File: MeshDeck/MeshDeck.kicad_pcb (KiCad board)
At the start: 4 copper layers, 48 parts, among them CN1 ATGM336H-6N-74, SW1 4*4*1.7, SW2 4*4*1.7, U1 ESP32-S3-WROOM-1(N16R8), U2 SX1262S8S+T-X1, U3 TPS6282533DMQR, U4 BQ24074RGTR, U5 RN32768114

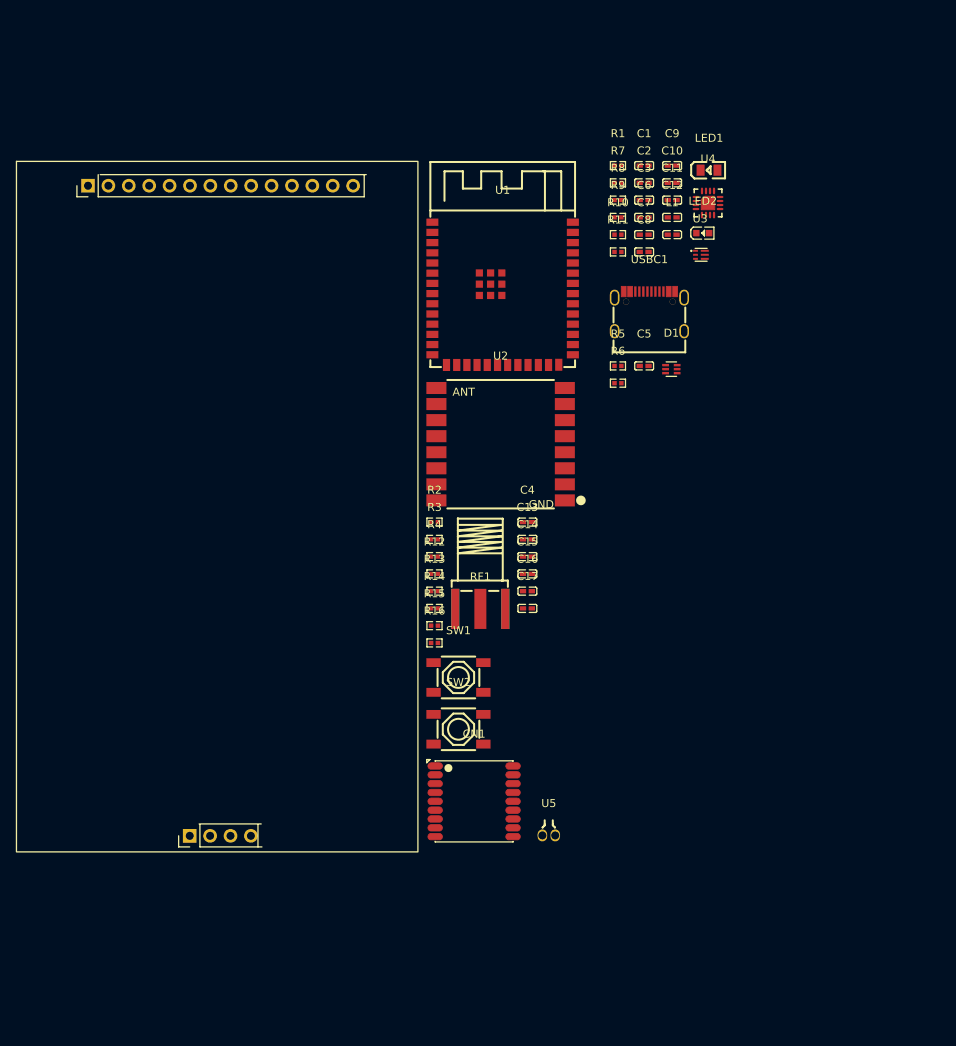
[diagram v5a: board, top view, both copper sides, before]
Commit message: Added GPS and sof power button
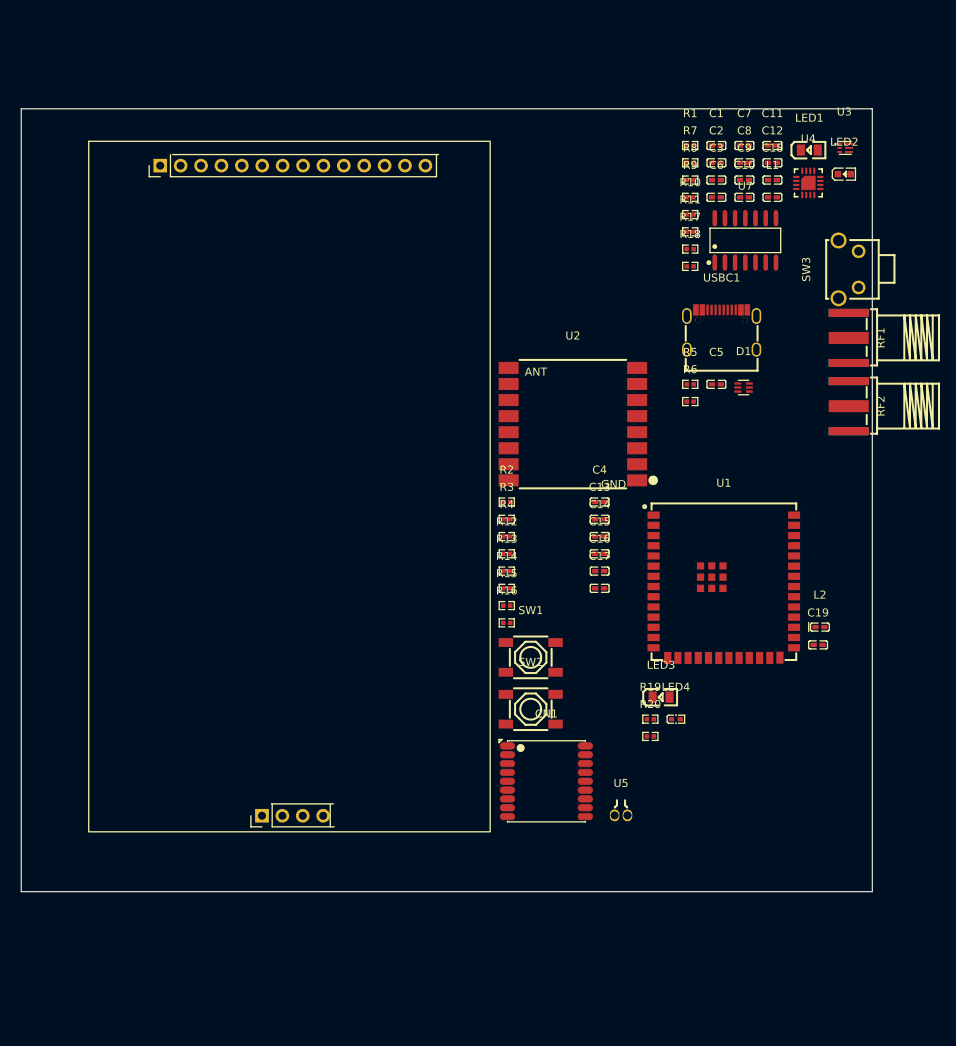
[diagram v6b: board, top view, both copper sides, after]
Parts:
- added C18: 1uF, MeshDeck:C0402, F.Cu at (183.6, 51.4)
- added C19: 10uF, MeshDeck:C0402, F.Cu at (189.2, 109.3)
- added L2: 47nH, MeshDeck:L0402-RD, F.Cu at (189.5, 107.0)
- added LED3: 0805G (Green), MeshDeck:LED0805-R-RD, F.Cu at (169.7, 115.8)
- added LED4: red, MeshDeck:LED0402-RD, F.Cu at (171.5, 118.5)
- added R17: 10KOhm, MeshDeck:R0402, F.Cu at (173.3, 60.0)
- added R18: 10KOhm, MeshDeck:R0402, F.Cu at (173.3, 62.1)
- added R19: 220ohm, MeshDeck:R0402, F.Cu at (168.3, 118.5)
- added R20: 220ohm, MeshDeck:R0402, F.Cu at (168.3, 120.7)
- added RF2: HJ-SMA023, MeshDeck:SMA-SMD_HJ-SMA023, F.Cu at (193.1, 79.5)
- added SW3: SKHHLVA010, MeshDeck:KEY-TH_4P-L7.5-W6.8-P4.50-LS7.2, F.Cu at (193.0, 62.5)
- added U7: CD4013BM, MeshDeck:SOIC-14_L8.7-W3.9-P1.27-LS6.0-BL, F.Cu at (180.2, 58.9)
- U1: value ESP32-S3-WROOM-1(N16R8) -> ESP32-S3-WROOM-1U-N16R8; footprint MeshDeck:WIRELM-SMD_ESP32-S3-WROOM-1 -> MeshDeck:WIRELM-SMD_ESP32-S3-WROOM-1U
- moved RF1 57.0 mm to (193.1, 71.0), turned to -90 degrees
- moved U1 45.7 mm to (177.5, 102.0)
- moved U3 22.4 mm to (192.5, 47.4)
- moved LED2 19.1 mm to (192.5, 50.6)
- moved C8 16.7 mm to (180.1, 49.2)
- moved C7 16.7 mm to (180.1, 47.1)
- moved C11 14.2 mm to (183.6, 47.1)
- moved C12 14.2 mm to (183.6, 49.2)
- moved L1 13.3 mm to (183.6, 53.5)
- moved LED1 12.7 mm to (188.1, 47.6)
- moved U4 12.7 mm to (188.0, 51.7)
- moved C1 9.34 mm to (176.6, 47.1)
- moved C13 9.34 mm to (162.0, 93.6)
- moved C14 9.34 mm to (162.0, 95.8)
- moved C15 9.34 mm to (162.0, 97.9)
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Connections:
- CN1 pad 1: unconnected-(CN1-GND-Pad1) -> GND
- CN1 pad 10: unconnected-(CN1-GND-Pad10) -> GND
- CN1 pad 11: unconnected-(CN1-RF_IN-Pad11) -> Net-(CN1-RF_IN)
- CN1 pad 12: unconnected-(CN1-GND-Pad12) -> GND
- CN1 pad 14: unconnected-(CN1-VCC_RF-Pad14) -> Net-(CN1-VCC_RF)
- CN1 pad 2: unconnected-(CN1-TXD0-Pad2) -> /RXD0_ESP
- CN1 pad 3: unconnected-(CN1-RXD0-Pad3) -> /RXD0_ESP
- CN1 pad 4: unconnected-(CN1-1PPS-Pad4) -> /IO3
- CN1 pad 5: unconnected-(CN1-ON/OFF-Pad5) -> /IO48
- CN1 pad 6: unconnected-(CN1-VBAT-Pad6) -> /3V3
- CN1 pad 8: unconnected-(CN1-VCC-Pad8) -> /3V3
- CN1 pad 9: unconnected-(CN1-nRESET-Pad9) -> /IO35
- U1 pad 15: unconnected-(U1-IO3-Pad15) -> /IO3
- U1 pad 16: unconnected-(U1-IO46-Pad16) -> GND
- U1 pad 18: unconnected-(U1-IO10-Pad18) -> /IO10
- U1 pad 23: unconnected-(U1-IO21-Pad23) -> /IO21
- U1 pad 24: unconnected-(U1-IO47-Pad24) -> /IO47
- U1 pad 25: unconnected-(U1-IO48-Pad25) -> /IO48
- U1 pad 28: unconnected-(U1-IO35-Pad28) -> /IO35
- U1 pad 36: unconnected-(U1-RXD0-Pad36) -> /RXD0_ESP
- U1 pad 37: unconnected-(U1-TXD0-Pad37) -> /RXD0_ESP
- U3 pad 1: /Power Sheet/BCC_OUT -> Net-(LED3-A)
- U6 pad 1: unconnected-(U6-VCC-Pad1) -> /3V3
- U6 pad 10: unconnected-(U6-T_CLK-Pad10) -> /SPI.SCK
- U6 pad 11: unconnected-(U6-T_CS-Pad11) -> /IO21
- U6 pad 12: unconnected-(U6-T_MOSI-Pad12) -> /SPI.MOSI
- U6 pad 13: unconnected-(U6-T_MISO-Pad13) -> /SPI.MISO
- U6 pad 14: unconnected-(U6-T_IRQ-Pad14) -> /IO47
- U6 pad 2: unconnected-(U6-GND-Pad2) -> GND
- U6 pad 4: unconnected-(U6-RESET-Pad4) -> /IO10
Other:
- board outline added: 106 x 97.5 mm

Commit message: added sd card and started keyboard
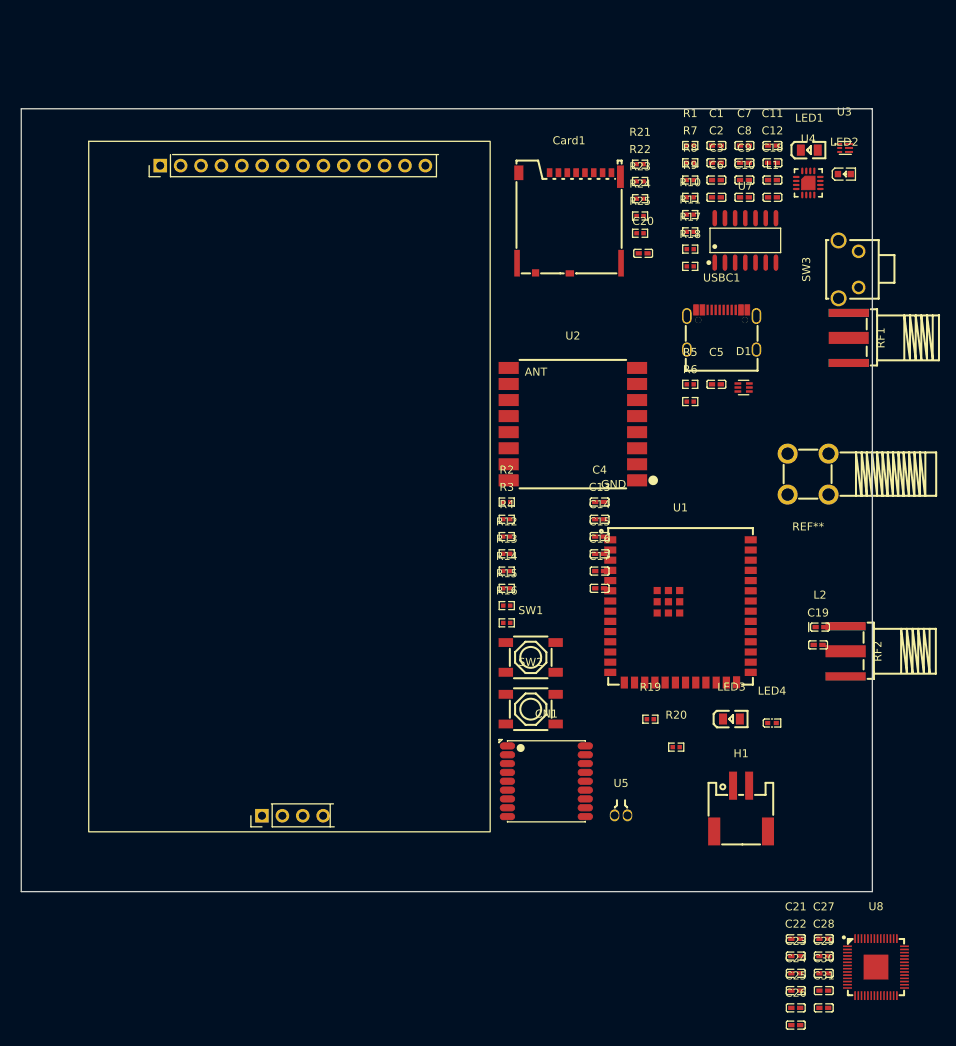
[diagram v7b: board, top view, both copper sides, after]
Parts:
- added C20: 0.1uF, MeshDeck:C0402, F.Cu at (167.4, 60.5)
- added C21: 1uF, MeshDeck:C0402, F.Cu at (186.5, 145.9)
- added C22: 0.1uF, MeshDeck:C0402, F.Cu at (186.5, 148.0)
- added C23: 0.1uF, MeshDeck:C0402, F.Cu at (186.5, 150.2)
- added C24: 0.1uF, MeshDeck:C0402, F.Cu at (186.5, 152.3)
- added C25: 0.1uF, MeshDeck:C0402, F.Cu at (186.5, 154.5)
- added C26: 0.1uF, MeshDeck:C0402, F.Cu at (186.5, 156.6)
- added C27: 0.1uF, MeshDeck:C0402, F.Cu at (189.9, 145.9)
- added C28: 0.1uF, MeshDeck:C0402, F.Cu at (189.9, 148.0)
- added C29: 1uF, MeshDeck:C0402, F.Cu at (189.9, 150.2)
- added C30: 0.1uF, MeshDeck:C0402, F.Cu at (189.9, 152.3)
- added C31: 0.1uF, MeshDeck:C0402, F.Cu at (189.9, 154.5)
- added Card1: 503398-1892, MeshDeck:TF-SMD_503398-1892, F.Cu at (158.2, 56.7)
- added H1: WAFER-PH2.0-2PWB, MeshDeck:CONN-SMD_2P-P2.00_XUNPU_WAFER-PH2.0-2PWB, F.Cu at (179.7, 129.7)
- added R21: 10KOhm, MeshDeck:R0402, F.Cu at (167.1, 49.4)
- added R22: 10KOhm, MeshDeck:R0402, F.Cu at (167.1, 51.5)
- added R23: 10KOhm, MeshDeck:R0402, F.Cu at (167.1, 53.7)
- added R24: 10KOhm, MeshDeck:R0402, F.Cu at (167.1, 55.9)
- added R25: 10KOhm, MeshDeck:R0402, F.Cu at (167.1, 58.0)
- added REF**: SMA-TH_HJ-SMA429, MeshDeck:SMA-TH_HJ-SMA429, F.Cu at (188.0, 88.0)
- added U8: RP2040, MeshDeck:LQFN-56_L7.0-W7.0-P0.4-EP, F.Cu at (196.4, 149.4)
- moved RF2 30.5 mm to (192.7, 110.1)
- moved LED4 12.0 mm to (183.5, 119.0)
- moved LED3 9.18 mm to (178.4, 118.5)
- moved U1 6.21 mm to (172.1, 105.1)
- moved R20 3.48 mm to (171.6, 122.0)
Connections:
- SW3 pad 2: Net-(LED4-A) -> /Power Sheet/CLOCK1
- U1 pad 29: unconnected-(U1-IO36-Pad29) -> /IO36
- U7 pad 3: Net-(LED4-A) -> /Power Sheet/CLOCK1

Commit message: started pcb plus pin socket for expansion
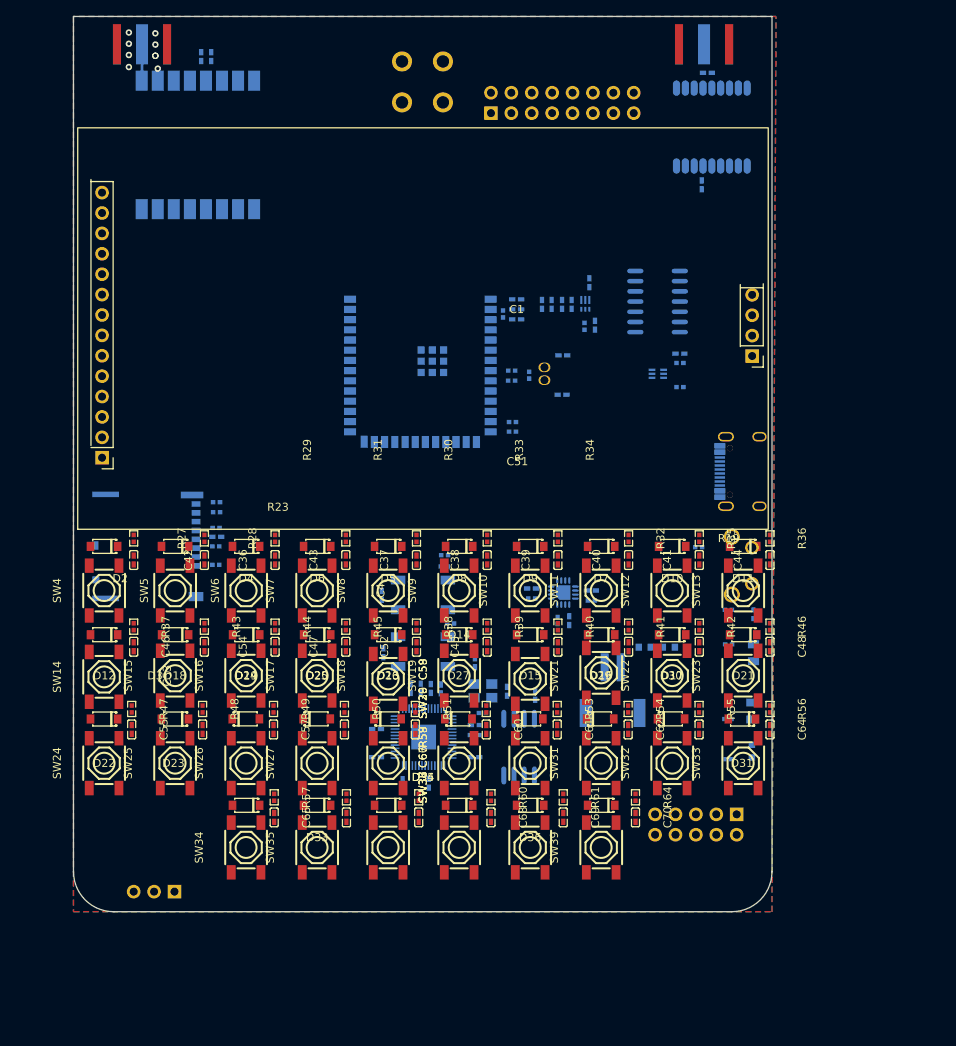
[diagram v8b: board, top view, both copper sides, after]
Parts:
- added C32: 0.1uF, MeshDeck:C0402, B.Cu at (154.0, 115.5)
- added C33: 15pF, MeshDeck:C0402, B.Cu at (146.5, 111.5)
- added C34: 15pF, MeshDeck:C0402, B.Cu at (150.5, 115.0)
- added C35: 0.1uF, MeshDeck:C0402, F.Cu at (104.0, 98.7)
- added C36: 0.1uF, MeshDeck:C0402, F.Cu at (121.6, 98.7)
- added C37: 0.1uF, MeshDeck:C0402, F.Cu at (139.2, 98.7)
- added C38: 0.1uF, MeshDeck:C0402, F.Cu at (148.0, 98.7)
- added C39: 0.1uF, MeshDeck:C0402, F.Cu at (156.8, 98.7)
- added C40: 0.1uF, MeshDeck:C0402, F.Cu at (165.6, 98.7)
- added C41: 0.1uF, MeshDeck:C0402, F.Cu at (174.4, 98.7)
- added C42: 0.1uF, MeshDeck:C0402, F.Cu at (112.8, 98.7)
- added C43: 0.1uF, MeshDeck:C0402, F.Cu at (130.4, 98.7)
- added C44: 0.1uF, MeshDeck:C0402, F.Cu at (183.2, 98.7)
- added C45: 0.1uF, MeshDeck:C0402, F.Cu at (148.0, 109.5)
- added C46: 0.1uF, MeshDeck:C0402, F.Cu at (104.0, 109.5)
- added C47: 0.1uF, MeshDeck:C0402, F.Cu at (130.4, 109.5)
- added C48: 0.1uF, MeshDeck:C0402, F.Cu at (183.2, 109.5)
- added C49: 0.1uF, MeshDeck:C0402, F.Cu at (174.4, 109.5)
- added C50: 0.1uF, MeshDeck:C0402, F.Cu at (165.6, 109.5)
- added C51: 0.1uF, MeshDeck:C0402, F.Cu at (156.8, 109.5)
- added C52: 0.1uF, MeshDeck:C0402, F.Cu at (139.2, 109.5)
- added C53: 0.1uF, MeshDeck:C0402, F.Cu at (112.8, 109.5)
- added C54: 0.1uF, MeshDeck:C0402, F.Cu at (121.6, 109.5)
- added C55: 0.1uF, MeshDeck:C0402, F.Cu at (103.8, 119.8)
- added C56: 0.1uF, MeshDeck:C0402, F.Cu at (112.6, 119.8)
- added C57: 0.1uF, MeshDeck:C0402, F.Cu at (121.4, 119.8)
- added C58: 0.1uF, MeshDeck:C0402, F.Cu at (130.2, 119.8)
- added C59: 0.1uF, MeshDeck:C0402, F.Cu at (139.1, 119.8)
- added C60: 0.1uF, MeshDeck:C0402, F.Cu at (147.9, 119.8)
- added C61: 0.1uF, MeshDeck:C0402, F.Cu at (156.8, 119.8)
- added C62: 0.1uF, MeshDeck:C0402, F.Cu at (165.6, 119.8)
- added C63: 0.1uF, MeshDeck:C0402, F.Cu at (174.4, 119.8)
- added C64: 0.1uF, MeshDeck:C0402, F.Cu at (183.2, 119.8)
- added C65: 0.1uF, MeshDeck:C0402, F.Cu at (121.5, 130.8)
- added C66: 0.1uF, MeshDeck:C0402, F.Cu at (130.5, 130.8)
- added C67: 0.1uF, MeshDeck:C0402, F.Cu at (139.5, 130.8)
- added C68: 0.1uF, MeshDeck:C0402, F.Cu at (148.5, 130.8)
- added C69: 0.1uF, MeshDeck:C0402, F.Cu at (157.5, 130.8)
- added C70: 0.1uF, MeshDeck:C0402, F.Cu at (166.5, 130.8)
- added D10: 1N4148W T4, MeshDeck:SOD-123_L2.8-W1.8-LS3.7-RD, F.Cu at (171.1, 97.0)
- added D11: 1N4148W T4, MeshDeck:SOD-123_L2.8-W1.8-LS3.7-RD, F.Cu at (179.9, 97.0)
- added D12: 1N4148W T4, MeshDeck:SOD-123_L2.8-W1.8-LS3.7-RD, F.Cu at (100.3, 108.0)
- added D13: 1N4148W T4, MeshDeck:SOD-123_L2.8-W1.8-LS3.7-RD, F.Cu at (135.7, 108.0)
- added D14: 1N4148W T4, MeshDeck:SOD-123_L2.8-W1.8-LS3.7-RD, F.Cu at (144.5, 108.0)
- added D15: 1N4148W T4, MeshDeck:SOD-123_L2.8-W1.8-LS3.7-RD, F.Cu at (153.4, 108.0)
- added D16: 1N4148W T4, MeshDeck:SOD-123_L2.8-W1.8-LS3.7-RD, F.Cu at (162.2, 108.0)
- added D17: 1N4148W T4, MeshDeck:SOD-123_L2.8-W1.8-LS3.7-RD, F.Cu at (171.1, 108.0)
- added D18: 1N4148W T4, MeshDeck:SOD-123_L2.8-W1.8-LS3.7-RD, F.Cu at (109.2, 108.0)
- added D19: 1N4148W T4, MeshDeck:SOD-123_L2.8-W1.8-LS3.7-RD, F.Cu at (118.0, 108.0)
- added D2: 1N4148W T4, MeshDeck:SOD-123_L2.8-W1.8-LS3.7-RD, F.Cu at (100.3, 97.0)
- added D20: 1N4148W T4, MeshDeck:SOD-123_L2.8-W1.8-LS3.7-RD, F.Cu at (126.8, 108.0)
- added D21: 1N4148W T4, MeshDeck:SOD-123_L2.8-W1.8-LS3.7-RD, F.Cu at (179.9, 108.0)
- added D22: 1N4148W T4, MeshDeck:SOD-123_L2.8-W1.8-LS3.7-RD, F.Cu at (100.3, 118.5)
- added D23: 1N4148W T4, MeshDeck:SOD-123_L2.8-W1.8-LS3.7-RD, F.Cu at (109.1, 118.5)
- added D24: 1N4148W T4, MeshDeck:SOD-123_L2.8-W1.8-LS3.7-RD, F.Cu at (118.0, 118.5)
- added D25: 1N4148W T4, MeshDeck:SOD-123_L2.8-W1.8-LS3.7-RD, F.Cu at (126.8, 118.5)
- added D26: 1N4148W T4, MeshDeck:SOD-123_L2.8-W1.8-LS3.7-RD, F.Cu at (135.6, 118.5)
- added D27: 1N4148W T4, MeshDeck:SOD-123_L2.8-W1.8-LS3.7-RD, F.Cu at (144.4, 118.5)
- added D28: 1N4148W T4, MeshDeck:SOD-123_L2.8-W1.8-LS3.7-RD, F.Cu at (153.3, 118.5)
- added D29: 1N4148W T4, MeshDeck:SOD-123_L2.8-W1.8-LS3.7-RD, F.Cu at (162.1, 118.5)
- added D3: 1N4148W T4, MeshDeck:SOD-123_L2.8-W1.8-LS3.7-RD, F.Cu at (109.2, 97.0)
- added D30: 1N4148W T4, MeshDeck:SOD-123_L2.8-W1.8-LS3.7-RD, F.Cu at (170.9, 118.5)
- added D31: 1N4148W T4, MeshDeck:SOD-123_L2.8-W1.8-LS3.7-RD, F.Cu at (179.8, 118.5)
- added D32: 1N4148W T4, MeshDeck:SOD-123_L2.8-W1.8-LS3.7-RD, F.Cu at (118.0, 129.2)
- added D33: 1N4148W T4, MeshDeck:SOD-123_L2.8-W1.8-LS3.7-RD, F.Cu at (126.8, 129.2)
- added D34: 1N4148W T4, MeshDeck:SOD-123_L2.8-W1.8-LS3.7-RD, F.Cu at (135.7, 129.2)
- added D35: 1N4148W T4, MeshDeck:SOD-123_L2.8-W1.8-LS3.7-RD, F.Cu at (144.5, 129.2)
- added D36: 1N4148W T4, MeshDeck:SOD-123_L2.8-W1.8-LS3.7-RD, F.Cu at (153.4, 129.2)
- added D37: 1N4148W T4, MeshDeck:SOD-123_L2.8-W1.8-LS3.7-RD, F.Cu at (162.2, 129.2)
- added D4: 1N4148W T4, MeshDeck:SOD-123_L2.8-W1.8-LS3.7-RD, F.Cu at (118.0, 97.0)
- added D5: 1N4148W T4, MeshDeck:SOD-123_L2.8-W1.8-LS3.7-RD, F.Cu at (135.7, 97.0)
- added D6: 1N4148W T4, MeshDeck:SOD-123_L2.8-W1.8-LS3.7-RD, F.Cu at (126.8, 97.0)
- added D7: 1N4148W T4, MeshDeck:SOD-123_L2.8-W1.8-LS3.7-RD, F.Cu at (162.2, 97.0)
- added D8: 1N4148W T4, MeshDeck:SOD-123_L2.8-W1.8-LS3.7-RD, F.Cu at (144.5, 97.0)
- added D9: 1N4148W T4, MeshDeck:SOD-123_L2.8-W1.8-LS3.7-RD, F.Cu at (153.4, 97.0)
- added J1: Conn_01x03_MountingPin, Connector_PinHeader_2.54mm:PinHeader_1x03_P2.54mm_Horizontal, B.Cu at (109.1, 140.0)
- added J2: Conn_02x05_Odd_Even, Connector_PinSocket_2.54mm:PinSocket_2x05_P2.54mm_Horizontal, B.Cu at (179.1, 130.4)
- added J3: Conn_02x08_Odd_Even, Connector_PinSocket_2.54mm:PinSocket_2x08_P2.54mm_Horizontal, B.Cu at (148.5, 43.0)
- added R26: 1k, MeshDeck:R0402, B.Cu at (147.4, 117.8)
- added R27: 1k, MeshDeck:R0402, F.Cu at (104.0, 96.0)
- added R28: 1k, MeshDeck:R0402, F.Cu at (112.8, 96.0)
- added R29: 1k, MeshDeck:R0402, F.Cu at (121.6, 96.0)
- added R30: 1k, MeshDeck:R0402, F.Cu at (139.2, 96.0)
- added R31: 1k, MeshDeck:R0402, F.Cu at (130.4, 96.0)
- added R32: 1k, MeshDeck:R0402, F.Cu at (165.6, 96.0)
- added R33: 1k, MeshDeck:R0402, F.Cu at (148.0, 96.0)
- added R34: 1k, MeshDeck:R0402, F.Cu at (156.8, 96.0)
- added R35: 1k, MeshDeck:R0402, F.Cu at (174.4, 96.0)
- added R36: 1k, MeshDeck:R0402, F.Cu at (183.2, 96.0)
- added R37: 1k, MeshDeck:R0402, F.Cu at (104.0, 107.0)
- added R38: 1k, MeshDeck:R0402, F.Cu at (139.2, 107.0)
- added R39: 1k, MeshDeck:R0402, F.Cu at (148.0, 107.0)
- added R40: 1k, MeshDeck:R0402, F.Cu at (156.8, 107.0)
- added R41: 1k, MeshDeck:R0402, F.Cu at (165.6, 107.0)
- added R42: 1k, MeshDeck:R0402, F.Cu at (174.4, 107.0)
- added R43: 1k, MeshDeck:R0402, F.Cu at (112.8, 107.0)
- added R44: 1k, MeshDeck:R0402, F.Cu at (121.6, 107.0)
- added R45: 1k, MeshDeck:R0402, F.Cu at (130.4, 107.0)
- added R46: 1k, MeshDeck:R0402, F.Cu at (183.2, 107.0)
- added R47: 1k, MeshDeck:R0402, F.Cu at (103.8, 117.2)
- added R48: 1k, MeshDeck:R0402, F.Cu at (112.6, 117.2)
- added R49: 1k, MeshDeck:R0402, F.Cu at (121.4, 117.2)
- added R50: 1k, MeshDeck:R0402, F.Cu at (130.2, 117.2)
- added R51: 1k, MeshDeck:R0402, F.Cu at (139.1, 117.2)
- added R52: 1k, MeshDeck:R0402, F.Cu at (147.9, 117.2)
- added R53: 1k, MeshDeck:R0402, F.Cu at (156.8, 117.2)
- added R54: 1k, MeshDeck:R0402, F.Cu at (165.6, 117.2)
- added R55: 1k, MeshDeck:R0402, F.Cu at (174.4, 117.2)
- added R56: 1k, MeshDeck:R0402, F.Cu at (183.2, 117.2)
- added R57: 1k, MeshDeck:R0402, F.Cu at (121.5, 128.2)
- added R58: 1k, MeshDeck:R0402, F.Cu at (130.5, 128.2)
- added R59: 1k, MeshDeck:R0402, F.Cu at (139.5, 128.2)
- added R60: 1k, MeshDeck:R0402, F.Cu at (148.5, 128.2)
- added R61: 1k, MeshDeck:R0402, F.Cu at (157.5, 128.2)
- added R62: 100k, MeshDeck:R0603, B.Cu at (167.7, 109.5)
- added R63: 100k, MeshDeck:R0603, B.Cu at (170.7, 109.5)
- added R64: 1k, MeshDeck:R0402, F.Cu at (166.5, 128.2)
- added SW10: 4*4*1.7, MeshDeck:SW-SMD_4P-L5.2-W5.2-P3.70-LS6.5, F.Cu at (153.4, 102.5)
- added SW11: 4*4*1.7, MeshDeck:SW-SMD_4P-L5.2-W5.2-P3.70-LS6.5, F.Cu at (162.2, 102.5)
- added SW12: 4*4*1.7, MeshDeck:SW-SMD_4P-L5.2-W5.2-P3.70-LS6.5, F.Cu at (171.1, 102.5)
- added SW13: 4*4*1.7, MeshDeck:SW-SMD_4P-L5.2-W5.2-P3.70-LS6.5, F.Cu at (179.9, 102.5)
- added SW14: 4*4*1.7, MeshDeck:SW-SMD_4P-L5.2-W5.2-P3.70-LS6.5, F.Cu at (100.3, 113.2)
- added SW15: 4*4*1.7, MeshDeck:SW-SMD_4P-L5.2-W5.2-P3.70-LS6.5, F.Cu at (109.2, 113.1)
- added SW16: 4*4*1.7, MeshDeck:SW-SMD_4P-L5.2-W5.2-P3.70-LS6.5, F.Cu at (118.0, 113.1)
- added SW17: 4*4*1.7, MeshDeck:SW-SMD_4P-L5.2-W5.2-P3.70-LS6.5, F.Cu at (126.8, 113.1)
- added SW18: 4*4*1.7, MeshDeck:SW-SMD_4P-L5.2-W5.2-P3.70-LS6.5, F.Cu at (135.7, 113.5)
- added SW19: 4*4*1.7, MeshDeck:SW-SMD_4P-L5.2-W5.2-P3.70-LS6.5, F.Cu at (144.5, 113.1)
- added SW20: 4*4*1.7, MeshDeck:SW-SMD_4P-L5.2-W5.2-P3.70-LS6.5, F.Cu at (153.4, 113.5)
- added SW21: 4*4*1.7, MeshDeck:SW-SMD_4P-L5.2-W5.2-P3.70-LS6.5, F.Cu at (162.2, 112.8)
- added SW22: 4*4*1.7, MeshDeck:SW-SMD_4P-L5.2-W5.2-P3.70-LS6.5, F.Cu at (171.1, 113.1)
- added SW23: 4*4*1.7, MeshDeck:SW-SMD_4P-L5.2-W5.2-P3.70-LS6.5, F.Cu at (179.9, 113.1)
- added SW24: 4*4*1.7, MeshDeck:SW-SMD_4P-L5.2-W5.2-P3.70-LS6.5, F.Cu at (100.3, 124.0)
- added SW25: 4*4*1.7, MeshDeck:SW-SMD_4P-L5.2-W5.2-P3.70-LS6.5, F.Cu at (109.2, 124.0)
- added SW26: 4*4*1.7, MeshDeck:SW-SMD_4P-L5.2-W5.2-P3.70-LS6.5, F.Cu at (118.0, 124.0)
- added SW27: 4*4*1.7, MeshDeck:SW-SMD_4P-L5.2-W5.2-P3.70-LS6.5, F.Cu at (126.8, 124.0)
- added SW28: 4*4*1.7, MeshDeck:SW-SMD_4P-L5.2-W5.2-P3.70-LS6.5, F.Cu at (135.7, 124.0)
- added SW29: 4*4*1.7, MeshDeck:SW-SMD_4P-L5.2-W5.2-P3.70-LS6.5, F.Cu at (144.5, 124.0)
- added SW30: 4*4*1.7, MeshDeck:SW-SMD_4P-L5.2-W5.2-P3.70-LS6.5, F.Cu at (153.4, 124.0)
- added SW31: 4*4*1.7, MeshDeck:SW-SMD_4P-L5.2-W5.2-P3.70-LS6.5, F.Cu at (162.2, 124.0)
- added SW32: 4*4*1.7, MeshDeck:SW-SMD_4P-L5.2-W5.2-P3.70-LS6.5, F.Cu at (171.1, 124.0)
- added SW33: 4*4*1.7, MeshDeck:SW-SMD_4P-L5.2-W5.2-P3.70-LS6.5, F.Cu at (179.9, 124.0)
- added SW34: 4*4*1.7, MeshDeck:SW-SMD_4P-L5.2-W5.2-P3.70-LS6.5, F.Cu at (118.0, 134.5)
- added SW35: 4*4*1.7, MeshDeck:SW-SMD_4P-L5.2-W5.2-P3.70-LS6.5, F.Cu at (126.8, 134.5)
- added SW36: 4*4*1.7, MeshDeck:SW-SMD_4P-L5.2-W5.2-P3.70-LS6.5, F.Cu at (135.7, 134.5)
- added SW37: 4*4*1.7, MeshDeck:SW-SMD_4P-L5.2-W5.2-P3.70-LS6.5, F.Cu at (144.5, 134.5)
- added SW38: 4*4*1.7, MeshDeck:SW-SMD_4P-L5.2-W5.2-P3.70-LS6.5, F.Cu at (153.4, 134.5)
- added SW39: 4*4*1.7, MeshDeck:SW-SMD_4P-L5.2-W5.2-P3.70-LS6.5, F.Cu at (162.2, 134.5)
- added SW4: 4*4*1.7, MeshDeck:SW-SMD_4P-L5.2-W5.2-P3.70-LS6.5, F.Cu at (100.3, 102.5)
- added SW5: 4*4*1.7, MeshDeck:SW-SMD_4P-L5.2-W5.2-P3.70-LS6.5, F.Cu at (109.2, 102.5)
- added SW6: 4*4*1.7, MeshDeck:SW-SMD_4P-L5.2-W5.2-P3.70-LS6.5, F.Cu at (118.0, 102.5)
- added SW7: 4*4*1.7, MeshDeck:SW-SMD_4P-L5.2-W5.2-P3.70-LS6.5, F.Cu at (126.8, 102.5)
- added SW8: 4*4*1.7, MeshDeck:SW-SMD_4P-L5.2-W5.2-P3.70-LS6.5, F.Cu at (135.7, 102.5)
- added SW9: 4*4*1.7, MeshDeck:SW-SMD_4P-L5.2-W5.2-P3.70-LS6.5, F.Cu at (144.5, 102.5)
- added U10: ABM8-272-T3_C20625731, MeshDeck:CRYSTAL-SMD_4P-L3.2-W2.5-BL, B.Cu at (147.5, 115.0)
- added U9: W25Q128JVSIQTR, MeshDeck:SOIC-8_L5.3-W5.3-P1.27-LS8.0-BL, B.Cu at (152.0, 122.0)
- C1, C10, C11, C12, C13, C14, C15, C16, C17, C18, C19, C2, C20, C21, C22, C23, C24, C25, C26, C27, C28, C29, C3, C30, C31, C4, C5, C6, C7, C8, C9, CN1, Card1, D1, H1, L1, L2, LED1, LED2, LED3, LED4, R1, R10, R11, R12, R13, R14, R15, R16, R17, R18, R19, R2, R20, R21, R22, R23, R24, R25, R3, R4, R5, R6, R7, R8, R9, REF**, RF1, RF2, SW1, SW2, SW3, U1, U2, U3, U4, U5, U7, U8, USBC1: moved to B.Cu
- moved RF1 95.3 mm to (105.0, 34.5), turned to 180 degrees
- moved CN1 84.1 mm to (176.0, 44.8), turned to 90 degrees
- moved C17 82.0 mm to (113.7, 36.0), turned to -90 degrees
- moved C16 81.1 mm to (112.4, 36.0), turned to -90 degrees
- moved RF2 77.6 mm to (175.0, 34.5), turned to 180 degrees
- moved R7 74.4 mm to (178.0, 123.5), turned to 180 degrees
- moved LED2 72.8 mm to (181.0, 122.5), turned to -90 degrees
- moved L2 70.4 mm to (175.4, 38.0), turned to 180 degrees
- moved LED1 70.2 mm to (181.0, 117.5), turned to -90 degrees
- moved REF** 68.5 mm to (140.0, 39.2), turned to -90 degrees
- moved R23 68.3 mm to (114.2, 97.0), turned to 180 degrees
- moved R21 68.3 mm to (114.3, 92.8), turned to 180 degrees
- moved R22 68.2 mm to (114.3, 94.7), turned to 180 degrees
- moved R8 67.3 mm to (178.0, 118.5)
- moved R25 67.1 mm to (114.2, 99.3), turned to 180 degrees
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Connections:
- net /IO0 renamed /BOOT
- net /IO12 renamed /SCR_CS
- net /IO13 renamed /LORA_BUSY
- net /IO14 renamed /LORA_TXEN
- net /IO17 renamed /LORA_RESET
- net /IO21 renamed /TCH_CS
- net /IO3 renamed /GPS_PPS
- net /IO35 renamed /BOOT_RESET
- net /IO36 renamed /SD_CS
- net /IO45 renamed /LORA_DIO1
- net /IO47 renamed /TCH_IRQ
- CN1 pad 2: /RXD0_ESP -> /LORA_CS
- CN1 pad 3: /RXD0_ESP -> /LORA_CS
- U1 pad 11: unconnected-(U1-IO18-Pad11) -> /IO18
- U1 pad 12: unconnected-(U1-IO8-Pad12) -> /KB_SDA
- U1 pad 17: /IO9 -> /KB_SCL
- U1 pad 30: unconnected-(U1-IO37-Pad30) -> /LORA_CS
- U1 pad 31: unconnected-(U1-IO38-Pad31) -> /IO38
- U1 pad 36: /RXD0_ESP -> /LORA_CS
- U1 pad 37: /RXD0_ESP -> /LORA_CS
- U1 pad 38: unconnected-(U1-IO2-Pad38) -> /IO2
- U1 pad 39: unconnected-(U1-IO1-Pad39) -> /IO1
- U1 pad 4: unconnected-(U1-IO4-Pad4) -> /BTR_LVL
- U1 pad 5: unconnected-(U1-IO5-Pad5) -> /IO5
- U1 pad 6: unconnected-(U1-IO6-Pad6) -> /IO6
- U1 pad 7: unconnected-(U1-IO7-Pad7) -> /IO7
- U2 pad 5: /IO9 -> /LORA_CS
- U8 pad 11: unconnected-(U8-GPIO8-Pad11) -> /Keyboard/COL3
- U8 pad 12: unconnected-(U8-GPIO9-Pad12) -> /Keyboard/COL4
- U8 pad 13: unconnected-(U8-GPIO10-Pad13) -> /Keyboard/COL5
- U8 pad 14: unconnected-(U8-GPIO11-Pad14) -> /Keyboard/COL6
- U8 pad 15: unconnected-(U8-GPIO12-Pad15) -> /Keyboard/COL7
- U8 pad 16: unconnected-(U8-GPIO13-Pad16) -> /Keyboard/COL8
- U8 pad 17: unconnected-(U8-GPIO14-Pad17) -> /Keyboard/COL9
- U8 pad 18: unconnected-(U8-GPIO15-Pad18) -> /Keyboard/COL10
- U8 pad 2: unconnected-(U8-GPIO0-Pad2) -> /Keyboard/GPBOOT
- U8 pad 20: unconnected-(U8-XIN-Pad20) -> /Keyboard/XIN
- U8 pad 21: unconnected-(U8-XOUT-Pad21) -> /Keyboard/XOUT
- U8 pad 24: unconnected-(U8-SWCLK-Pad24) -> Net-(J1-Pin_3)
- U8 pad 25: unconnected-(U8-SWD-Pad25) -> Net-(J1-Pin_1)
- U8 pad 27: unconnected-(U8-GPIO16-Pad27) -> /Keyboard/ROW1
- U8 pad 28: unconnected-(U8-GPIO17-Pad28) -> /Keyboard/ROW2
- U8 pad 29: unconnected-(U8-GPIO18-Pad29) -> /Keyboard/ROW3
- U8 pad 3: unconnected-(U8-GPIO1-Pad3) -> /Keyboard/GPIO1
- U8 pad 30: unconnected-(U8-GPIO19-Pad30) -> /Keyboard/ROW4
- U8 pad 31: unconnected-(U8-GPIO20-Pad31) -> /Keyboard/GPIO20
- U8 pad 32: unconnected-(U8-GPIO21-Pad32) -> /Keyboard/GPTCH_CS
- U8 pad 34: unconnected-(U8-GPIO22-Pad34) -> /Keyboard/GPIO22
- U8 pad 35: unconnected-(U8-GPIO23-Pad35) -> /Keyboard/GPIO23
- U8 pad 36: unconnected-(U8-GPIO24-Pad36) -> /Keyboard/GPIO24
- U8 pad 37: unconnected-(U8-GPIO25-Pad37) -> /Keyboard/GPIO25
- U8 pad 38: unconnected-(U8-GPIO26_ADC0-Pad38) -> /Keyboard/GPIO26_ADC0
- U8 pad 39: unconnected-(U8-GPIO27_ADC1-Pad39) -> /Keyboard/GPIO27_ADC1
- U8 pad 4: unconnected-(U8-GPIO2-Pad4) -> /Keyboard/GPIO2
- U8 pad 40: unconnected-(U8-GPIO28_ADC2-Pad40) -> /Keyboard/GPIO28_ADC2
- U8 pad 41: unconnected-(U8-GPIO29_ADC3-Pad41) -> /Keyboard/GPIO29_ADC3
- U8 pad 5: unconnected-(U8-GPIO3-Pad5) -> /Keyboard/GPGPS_PPS
- U8 pad 51: unconnected-(U8-QSPI_SD3-Pad51) -> /Keyboard/QSPI_SD3
- U8 pad 52: unconnected-(U8-QSPI_SCLK-Pad52) -> /Keyboard/QSPI_SCLK
- U8 pad 53: unconnected-(U8-QSPI_SD0-Pad53) -> /Keyboard/QSPI_SD0
- U8 pad 54: unconnected-(U8-QSPI_SD2-Pad54) -> /Keyboard/QSPI_SD2
- U8 pad 55: unconnected-(U8-QSPI_SD1-Pad55) -> /Keyboard/QSPI_SD1
- U8 pad 56: unconnected-(U8-QSPI_SS-Pad56) -> /3V3
- U8 pad 6: unconnected-(U8-GPIO4-Pad6) -> /KB_SDA
- U8 pad 7: unconnected-(U8-GPIO5-Pad7) -> /KB_SCL
- U8 pad 8: unconnected-(U8-GPIO6-Pad8) -> /Keyboard/COL1
- U8 pad 9: unconnected-(U8-GPIO7-Pad9) -> /Keyboard/COL2
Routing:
- net Net-(RF1-SIG): track 0.00 -> 4.61 mm
- net /LORA_DIO1: track 0.00 -> 0.50 mm
- net GND: vias 0 -> 9
- added copper zone on B.Cu, net GND
- added copper zone on F.Cu, net GND
- added copper zone on In1.Cu, net GND
- added copper zone on In2.Cu, net GND
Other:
- board size 106 x 97.5 mm -> 87 x 111.5 mm
- board text added: "${REFERENCE}"
